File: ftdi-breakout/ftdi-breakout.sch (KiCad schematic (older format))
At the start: 17 parts, among them J1 Conn_01x06, J2 USB_C_Receptacle_USB2.0, U1 FT231XS

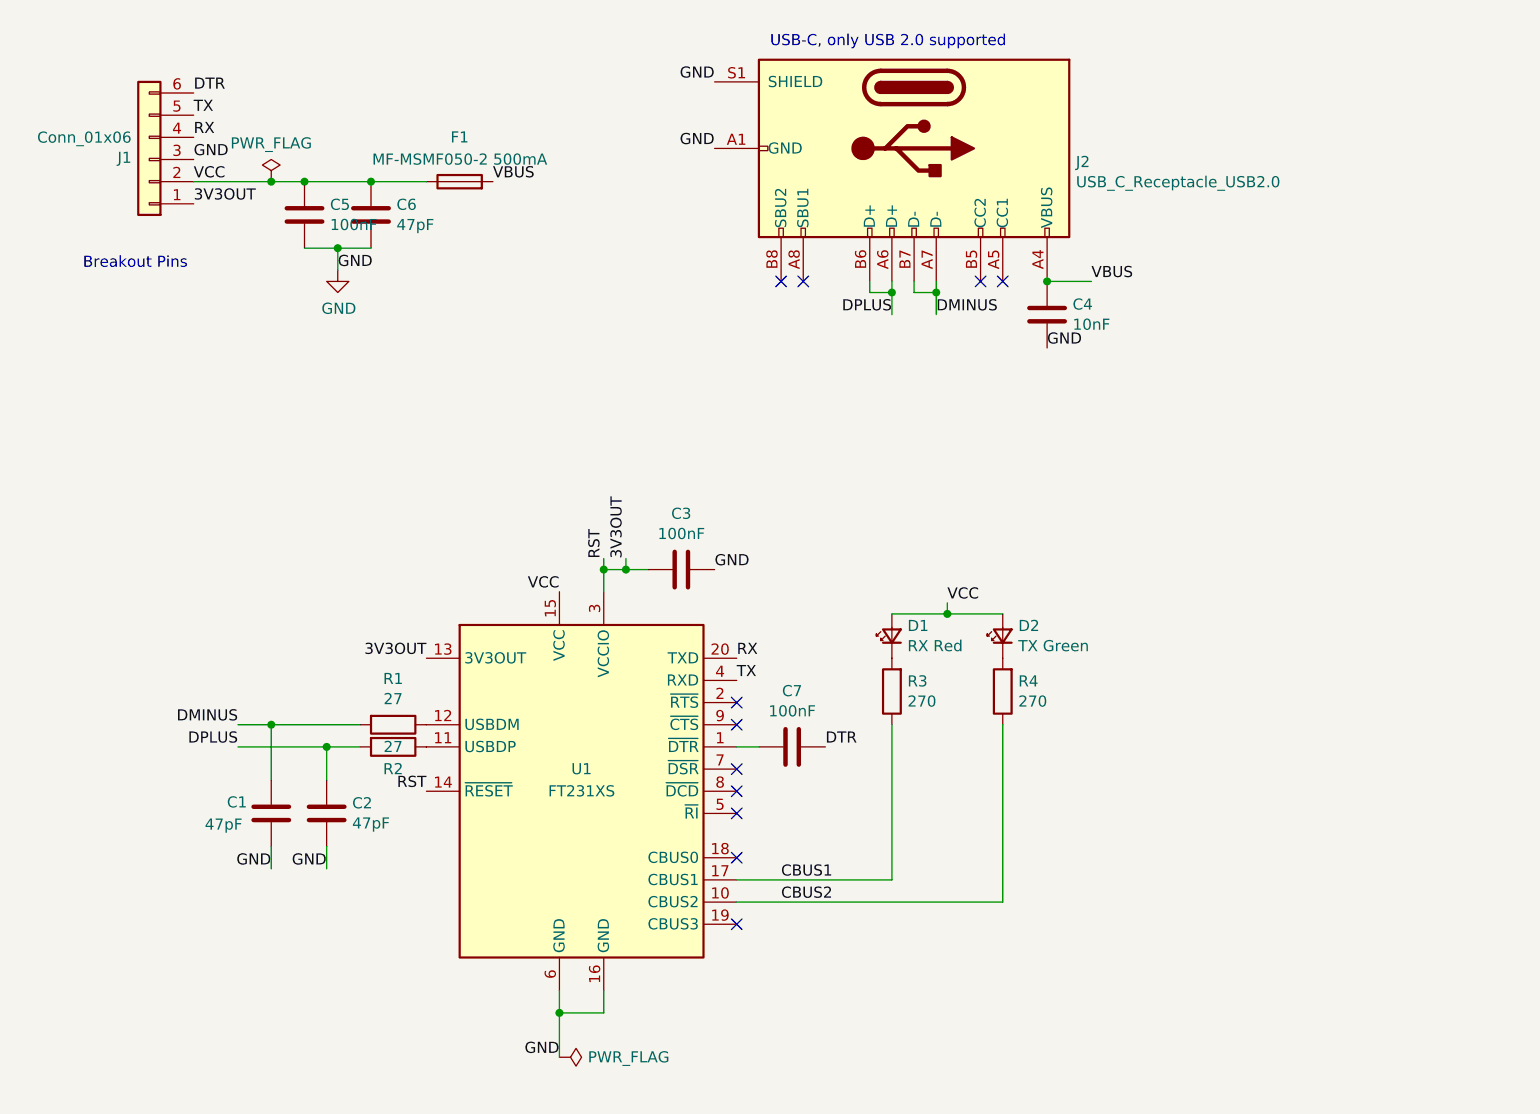
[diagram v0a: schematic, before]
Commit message: 🐛 [ftdi-breakout] Add missing resistors for CC1/CC2 USB-C connector and attach TX/RX LEDs to 3v3out
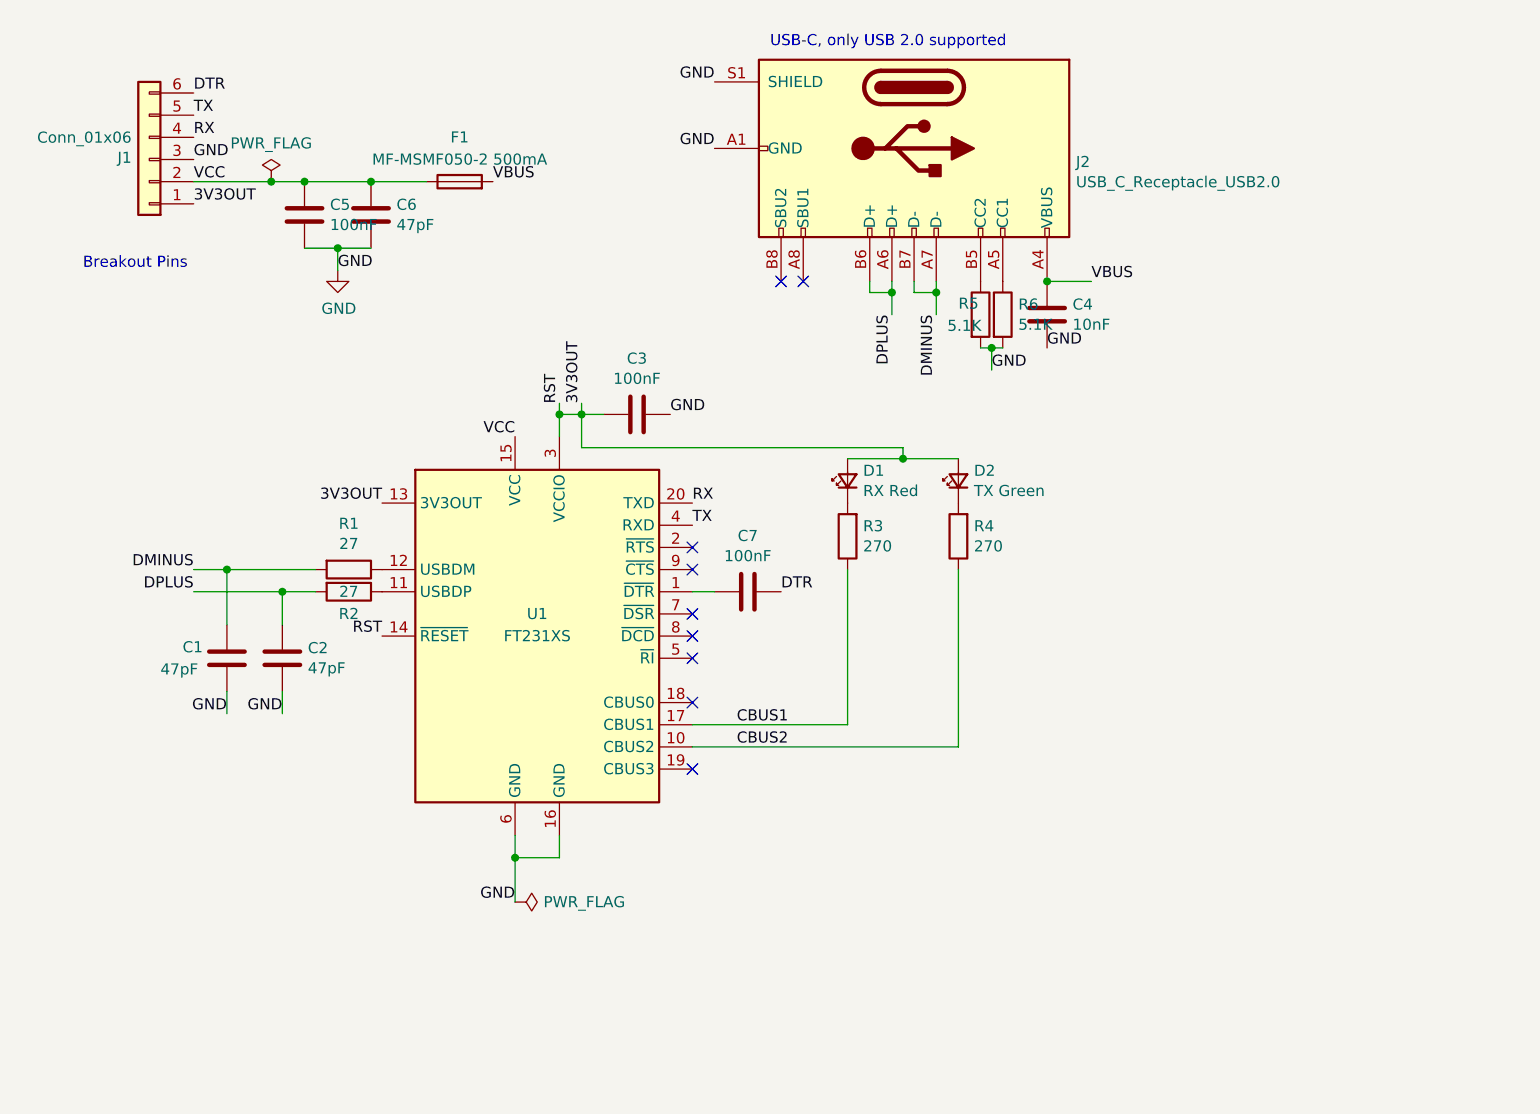
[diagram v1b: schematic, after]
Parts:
- added R5, R6: 5.1K, Resistor_SMD:R_0805_2012Metric_Pad1.20x1.40mm_HandSolder, symbol Device:R
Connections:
- net 3V3OUT: now also D1.2 (A), D2.2 (A)
- net GND: now also R5.2, R6.2
- net VCC: no longer D1.2 (A), D2.2 (A)
- net at J2.A5 (CC1): now also R6.1
- net at J2.B5 (CC2): now also R5.1
- no-connect marks 11 -> 9
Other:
- moved on the sheet: C1, C2, C3, C7, D1, D2, R1, R2, R3, R4, U1

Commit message: 🏗 [ftdi-breakout] Revision 2
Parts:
- removed C7: 100nF, Capacitor_SMD:C_0805_2012Metric_Pad1.18x1.45mm_HandSolder, symbol Device:C
- removed F1: MF-MSMF050-2 500mA, Fuse:Fuse_0805_2012Metric_Pad1.15x1.40mm_HandSolder, symbol Device:Fuse
- added D3: RX Red, LED_SMD:LED_0805_2012Metric_Pad1.15x1.40mm_HandSolder, symbol Device:LED_Small
- added R7: 270, Resistor_SMD:R_0805_2012Metric_Pad1.20x1.40mm_HandSolder, symbol Device:R
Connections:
- net VCC is gone; now on net VBUS: C5.1, C6.1, J1.2 (Pin_2), U1.15 (VCC)
- net DTR: now also U1.1 (~DTR)
- net GND: now also R7.1
- net RX: now also J1.5 (Pin_5), U1.4 (RXD); no longer J1.4 (Pin_4), U1.20 (TXD)
- net TX: now also J1.4 (Pin_4), U1.20 (TXD); no longer J1.5 (Pin_5), U1.4 (RXD)
- net VBUS: now also D3.2 (A)
- net DMINUS renamed D-
- net DPLUS renamed D+
- new net: D3.1 (K), R7.2
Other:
- moved on the sheet: C1, C2, C3, C4, C5, C6, D1, D2, J1, J2, R1, R2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
